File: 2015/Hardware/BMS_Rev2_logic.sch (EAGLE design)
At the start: 44 parts, among them Q9 MOSFET-NCHANNEL2N7002PW

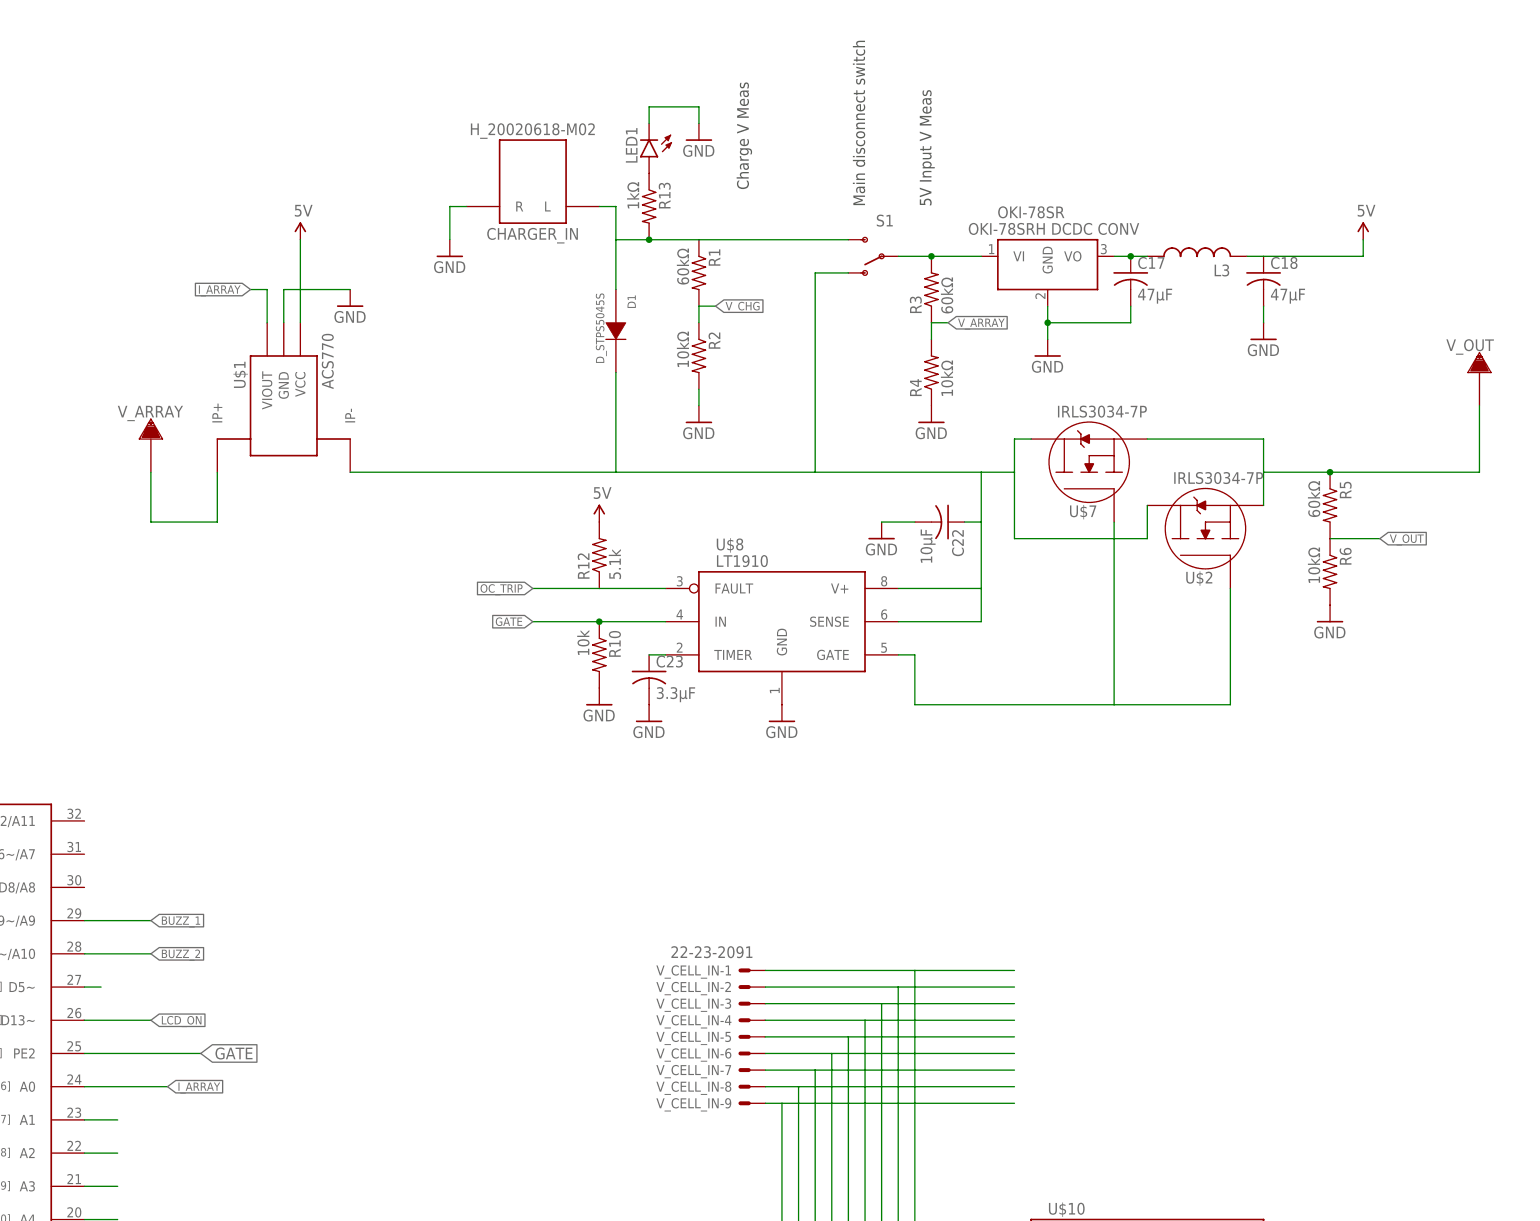
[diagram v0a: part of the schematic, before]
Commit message: Rev 2 work
Added documentation for Rev 2 and continued work on Rev 2.
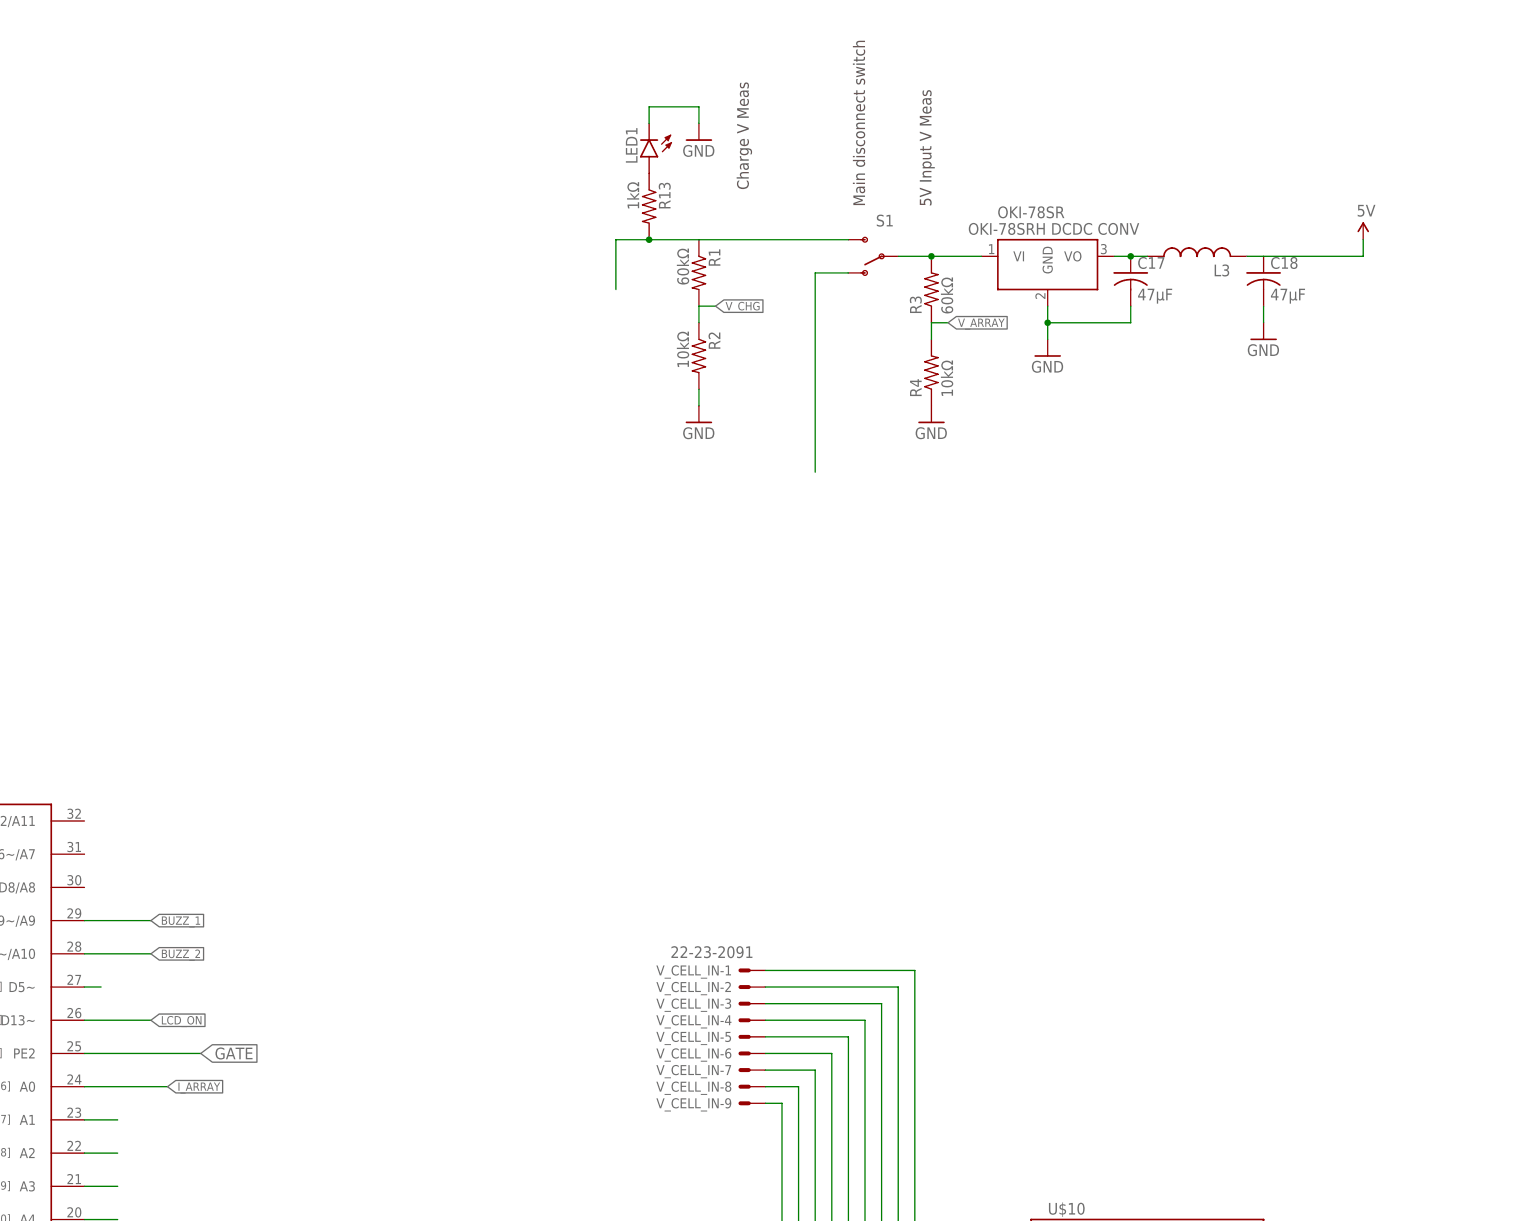
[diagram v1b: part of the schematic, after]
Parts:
- removed C22: 10µF, resistor:C-USC1206
- removed C23: 3.3µF, resistor:C-USC1206
- removed CHARGER_IN: H_20020618-M02, MRDT-2015-PowerBoard:H_20020618-M02
- removed D1: D_STPS5045S, MRDT-2015-BMS:D_STPS5045S
- removed R10: 10k, resistor:R-US_R1206
- removed R12: 5.1k, resistor:R-US_R1206
- removed R5: 60kΩ, resistor:R-US_R1206
- removed R6: 10kΩ, resistor:R-US_R1206
- removed U$1: ACS770, MRDT-2015-BMS:ACS770
- removed U$2, U$7: (no value), MRDT-2015-BMS:IRLS3034-7P
- removed U$8: LT1910, MRDT-2015-PowerBoard:LT1910
- removed V_ARRAY, V_OUT: TERMINAL_HOLE, MRDT-2015-PowerBoard:TERMINAL_HOLE
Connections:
- removed net N$1: R5.1, U$2.SOURCE, U$7.SOURCE, V_OUT.P$1
- removed net N$2: U$1.IP+, V_ARRAY.P$1
- removed net N$3: C22.1, D1.K, S1.O, U$1.IP-, U$2.DRAIN, U$7.DRAIN, U$8.SENSE, U$8.V+
- removed net N$31: C23.1, U$8.TIMER
- removed net OC_TRIP: R12.1, U$8.FAULT
- removed net V_OUT: R5.2, R6.1
- net 5V: no longer R12.2, U$1.VCC
- net GATE: no longer R10.1, U$8.IN
- net GND: no longer C22.2, C23.2, CHARGER_IN.R, R10.2, R6.2, U$1.GND, U$8.GND
- net I_ARRAY: no longer U$1.VIOUT
- net N$5: now also S1.O; no longer U$2.GATE, U$7.GATE, U$8.GATE
- net N$8: no longer CHARGER_IN.L, D1.A

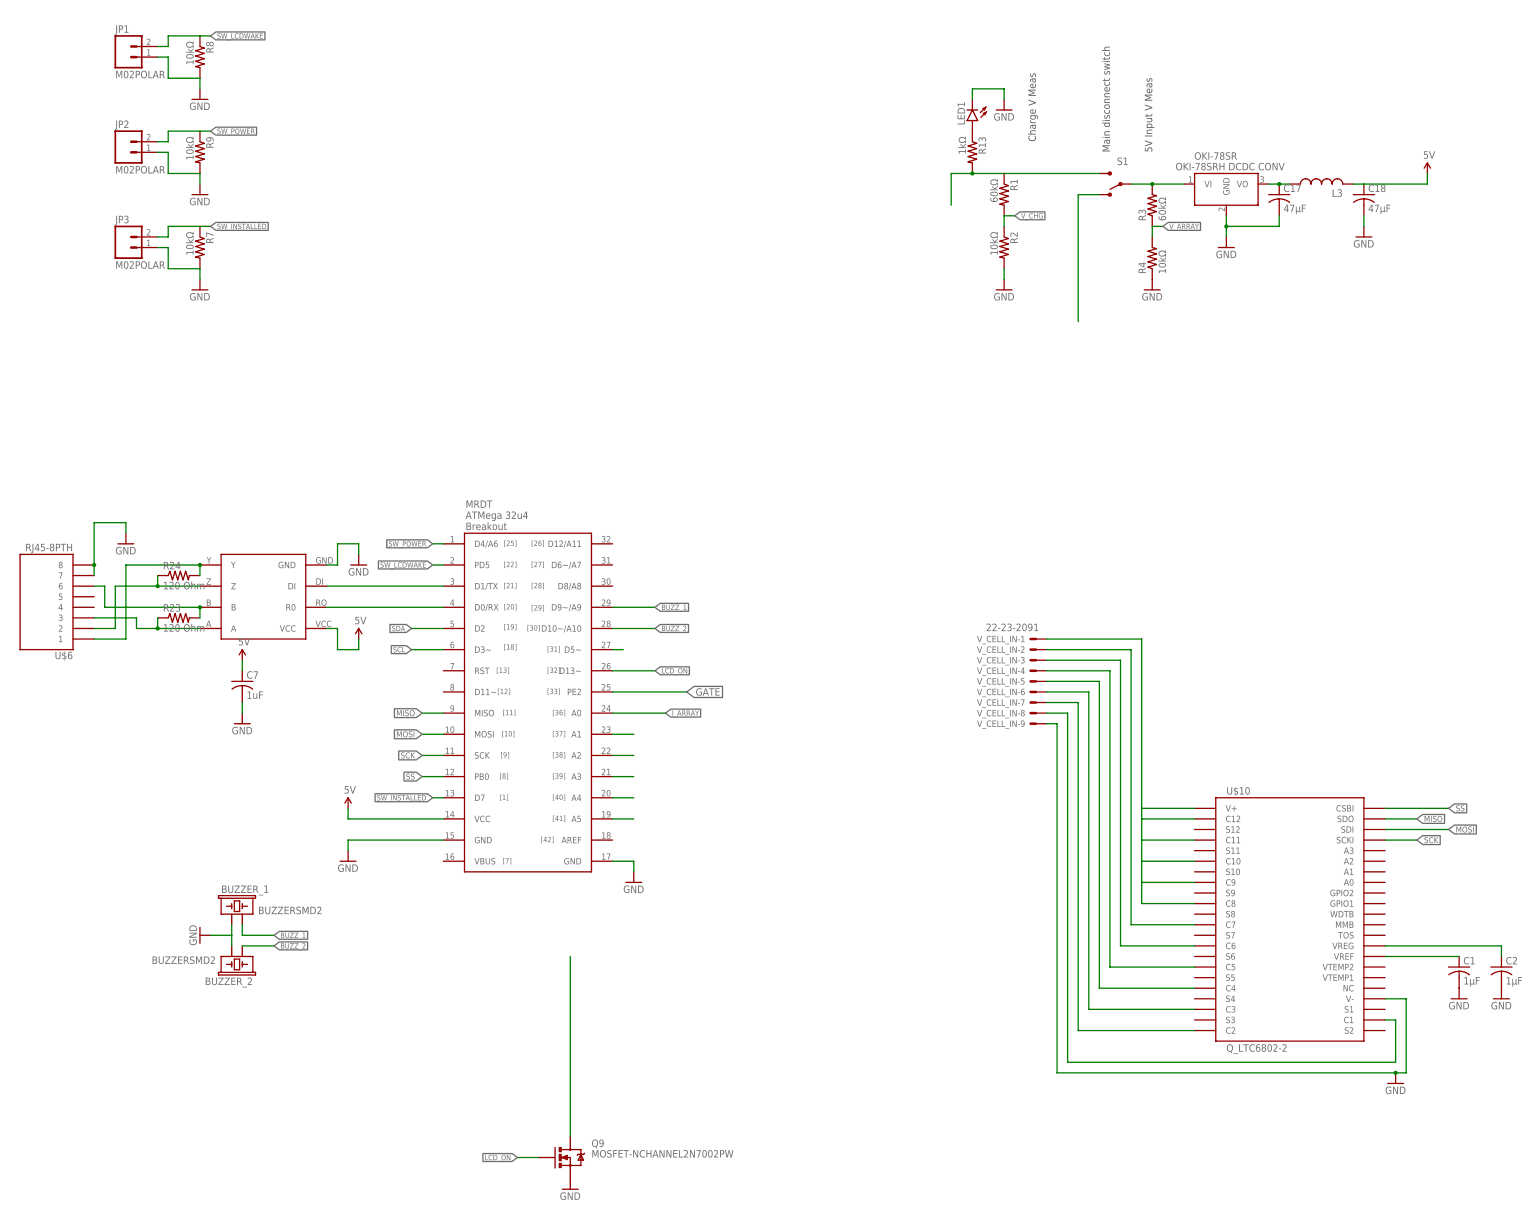
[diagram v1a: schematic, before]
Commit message: Worked on logic board
Added PTCs to the balance charger connection.
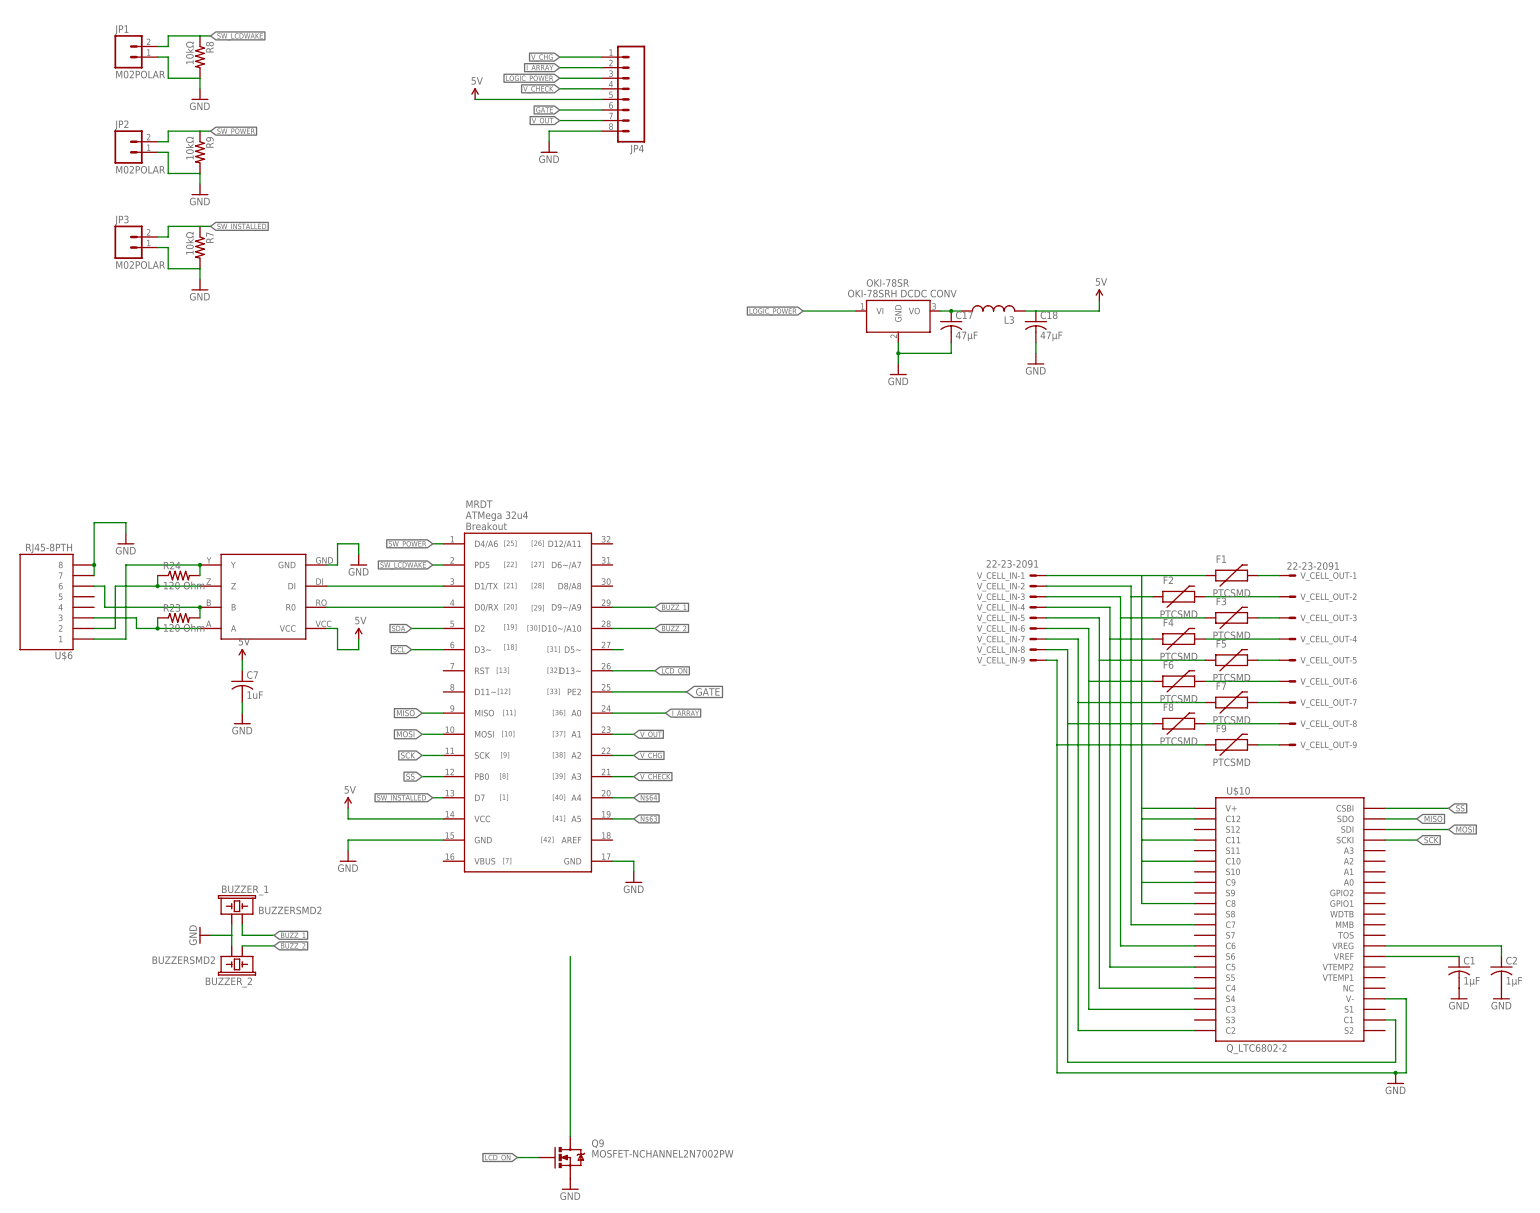
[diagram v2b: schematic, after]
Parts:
- removed LED1: (no value), SparkFun-LED:LED1206
- removed R1, R3: 60kΩ, resistor:R-US_R1206
- removed R13: 1kΩ, resistor:R-US_R1206
- removed R2, R4: 10kΩ, resistor:R-US_R1206
- removed S1: (no value), SparkFun-Electromechanical:SWITCH-SPDTPTH
- added F1, F2, F3, F4, F5, F6, F7, F8, F9: PTCSMD, SparkFun-PowerIC:PTCSMD
- added JP4: (no value), SparkFun-Connectors:M08BM08B-SRSS-TB
- added V_CELL_OUT: 22-23-2091, con-molex:22-23-2091
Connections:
- removed net N$34: LED1.A, R13.1
- removed net N$35: U$3.A1
- removed net N$36: U$3.A2
- removed net N$37: U$3.A3
- removed net N$5: S1.O
- removed net N$8: R1.1, R13.2, S1.S
- removed net V_ARRAY: R3.1, R4.2
- new net LOGIC_POWER: JP4.3, OKI-78SR.VI
- new net N$1: F1.2, V_CELL_OUT-1.S
- new net N$14: F4.2, V_CELL_OUT-4.S
- new net N$15: F5.2, V_CELL_OUT-5.S
- new net N$16: F6.2, V_CELL_OUT-6.S
- new net N$17: F7.2, V_CELL_OUT-7.S
- new net N$18: F8.2, V_CELL_OUT-8.S
- new net N$2: F2.2, V_CELL_OUT-2.S
- new net N$3: F3.2, V_CELL_OUT-3.S
- new net V_CHECK: JP4.4, U$3.A3
- new net V_OUT: JP4.7, U$3.A1
- net 5V: now also JP4.5
- net GATE: now also JP4.6
- net GND: now also F9.1, JP4.8; no longer LED1.C, R2.2, R4.1
- net I_ARRAY: now also JP4.2
- net N$4: now also F9.2, V_CELL_OUT-9.S; no longer OKI-78SR.VI, R3.2, S1.P
- net N$41: now also F1.1
- net N$42: now also F2.1
- net N$43: now also F3.1
- net N$46: now also F6.1
- net N$47: now also F7.1
- net N$48: now also F8.1
- net N$89: now also F4.1
- net N$91: now also F5.1
- net V_CHG: now also JP4.1, U$3.A2; no longer R1.2, R2.1
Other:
- note removed: "5V Input V Meas"
- note removed: "Charge V Meas"
- note removed: "Main disconnect switch"
- moved on the sheet: C17, C18, L3, OKI-78SR, V_CELL_IN-1, V_CELL_IN-2, V_CELL_IN-3, V_CELL_IN-4, V_CELL_IN-5, V_CELL_IN-6, V_CELL_IN-7, V_CELL_IN-8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
